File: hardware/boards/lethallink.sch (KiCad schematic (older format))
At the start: 11 parts, among them J1 PCIe-x4

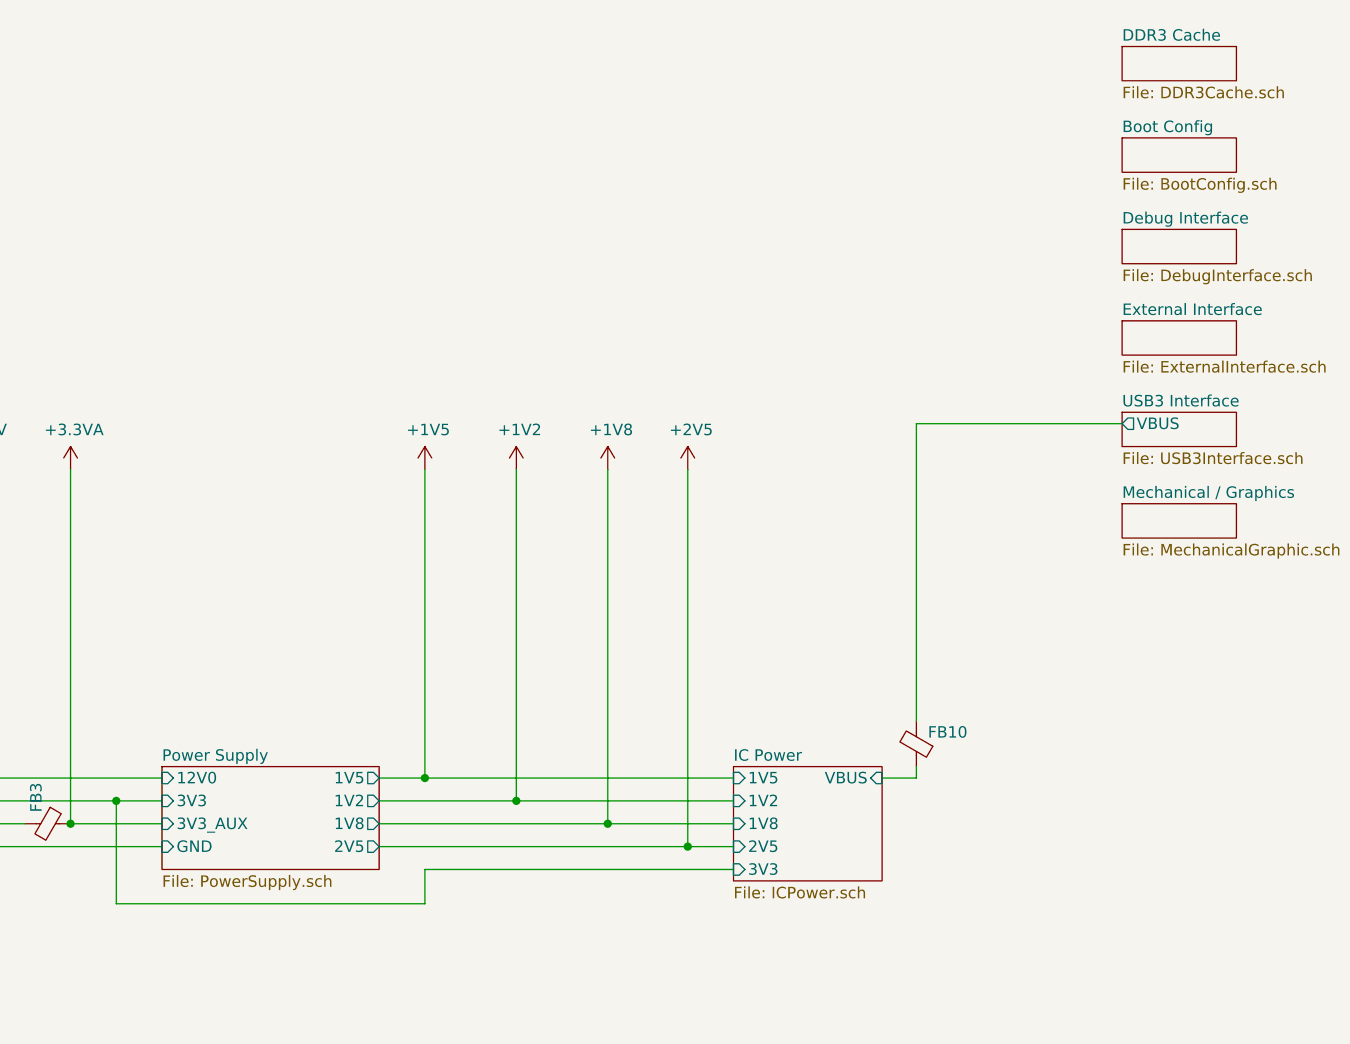
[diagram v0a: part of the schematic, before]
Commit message: Added the JTAG header and some misc cleanup
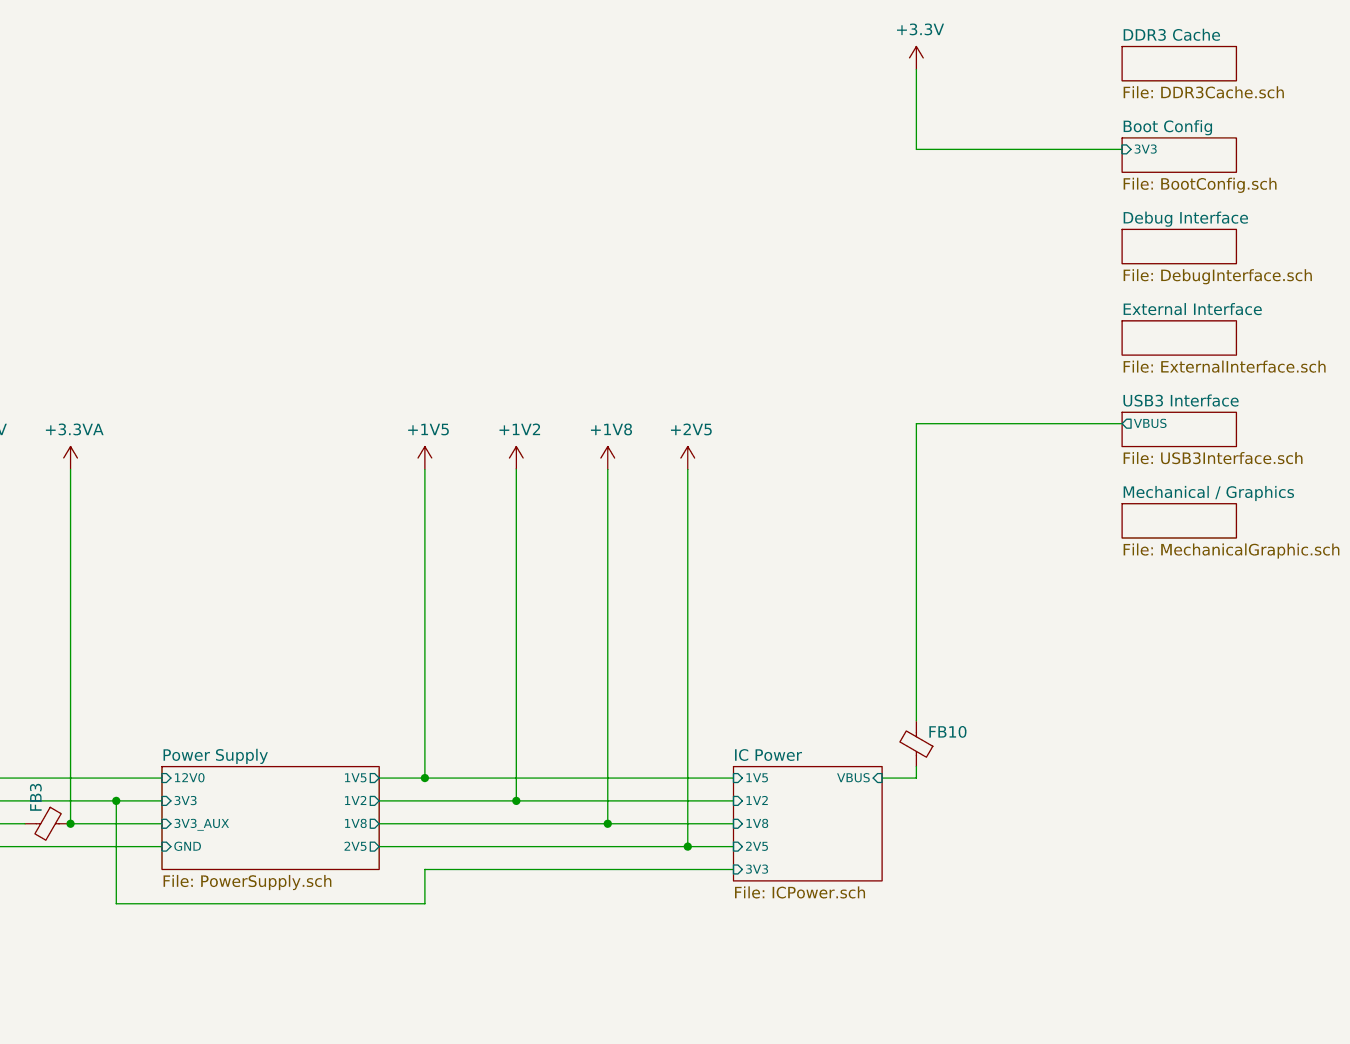
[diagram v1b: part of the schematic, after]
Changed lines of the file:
@@
 F0 "USB3 Interface" 50
 F1 "USB3Interface.sch" 50
-F2 "VBUS" O L 14700 2350 50
+F2 "VBUS" O L 14700 2350 39
 $EndSheet
 $Sheet
@@
 F0 "IC Power" 50
 F1 "ICPower.sch" 50
-F2 "3V3" I L 13000 4300 50
-F3 "1V8" I L 13000 4100 50
-F4 "2V5" I L 13000 4200 50
-F5 "1V2" I L 13000 4000 50
-F6 "1V5" I L 13000 3900 50
-F7 "VBUS" I R 13650 3900 50
+F2 "3V3" I L 13000 4300 39
+F3 "1V8" I L 13000 4100 39
+F4 "2V5" I L 13000 4200 39
+F5 "1V2" I L 13000 4000 39
+F6 "1V5" I L 13000 3900 39
+F7 "VBUS" I R 13650 3900 39
 $EndSheet
 $Comp
@@
 F0 "Power Supply" 50
 F1 "PowerSupply.sch" 50
-F2 "12V0" I L 10500 3900 50
-F3 "3V3" I L 10500 4000 50
-F4 "3V3_AUX" I L 10500 4100 50
-F5 "GND" I L 10500 4200 50
-F6 "1V2" O R 11450 4000 50
-F7 "2V5" O R 11450 4200 50
-F8 "1V8" O R 11450 4100 50
-F9 "1V5" O R 11450 3900 50
+F2 "12V0" I L 10500 3900 39
+F3 "3V3" I L 10500 4000 39
+F4 "3V3_AUX" I L 10500 4100 39
+F5 "GND" I L 10500 4200 39
+F6 "1V2" O R 11450 4000 39
+F7 "2V5" O R 11450 4200 39
+F8 "1V8" O R 11450 4100 39
+F9 "1V5" O R 11450 3900 39
 $EndSheet
 Wire Wire Line
@@
 	1    0    0    -1
 $EndComp
-$Sheet
-S 14700 1100 500  150
-U 5EF66251
-F0 "Boot Config" 50
-F1 "BootConfig.sch" 50
-$EndSheet
 Connection ~ 8950 4200
 $Comp
@@
 F1 "DDR3Cache.sch" 50
 $EndSheet
+$Sheet
+S 14700 1100 500  150
+U 5EF66251
+F0 "Boot Config" 50
+F1 "BootConfig.sch" 50
+F2 "3V3" I L 14700 1150 39
+$EndSheet
+Wire Wire Line
+	13800 800  13800 1150
+$Comp
+L power:+3.3V #PWR0126
+U 1 1 5FDBB3B1
+P 13800 800
+F 0 "#PWR0126" H 13800 650 50  0001 C CNN
+F 1 "+3.3V" H 13815 973 50  0000 C CNN
+F 2 "" H 13800 800 50  0001 C CNN
+F 3 "" H 13800 800 50  0001 C CNN
+	1    13800 800
+	1    0    0    -1
+$EndComp
+Wire Wire Line
+	13800 1150 14700 1150
 $EndSCHEMATC

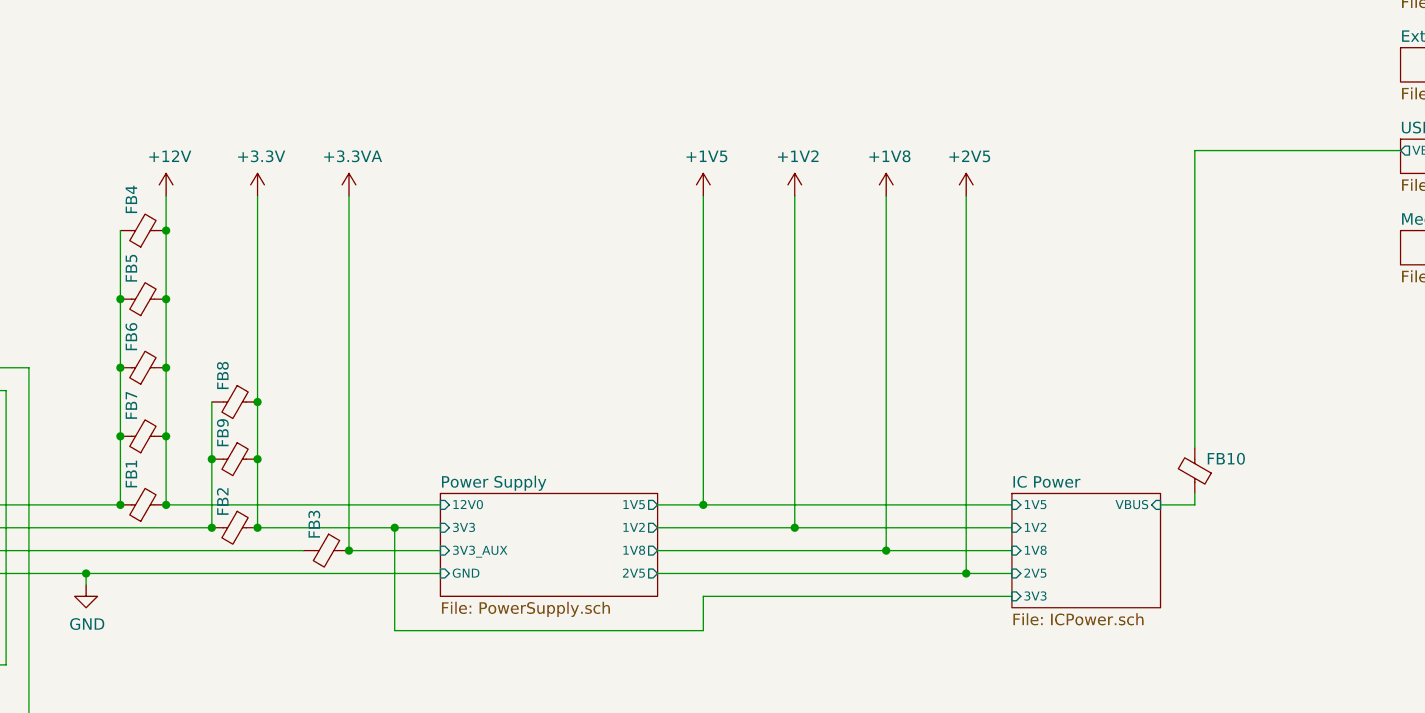
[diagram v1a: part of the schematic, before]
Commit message: Some ERC cleanup
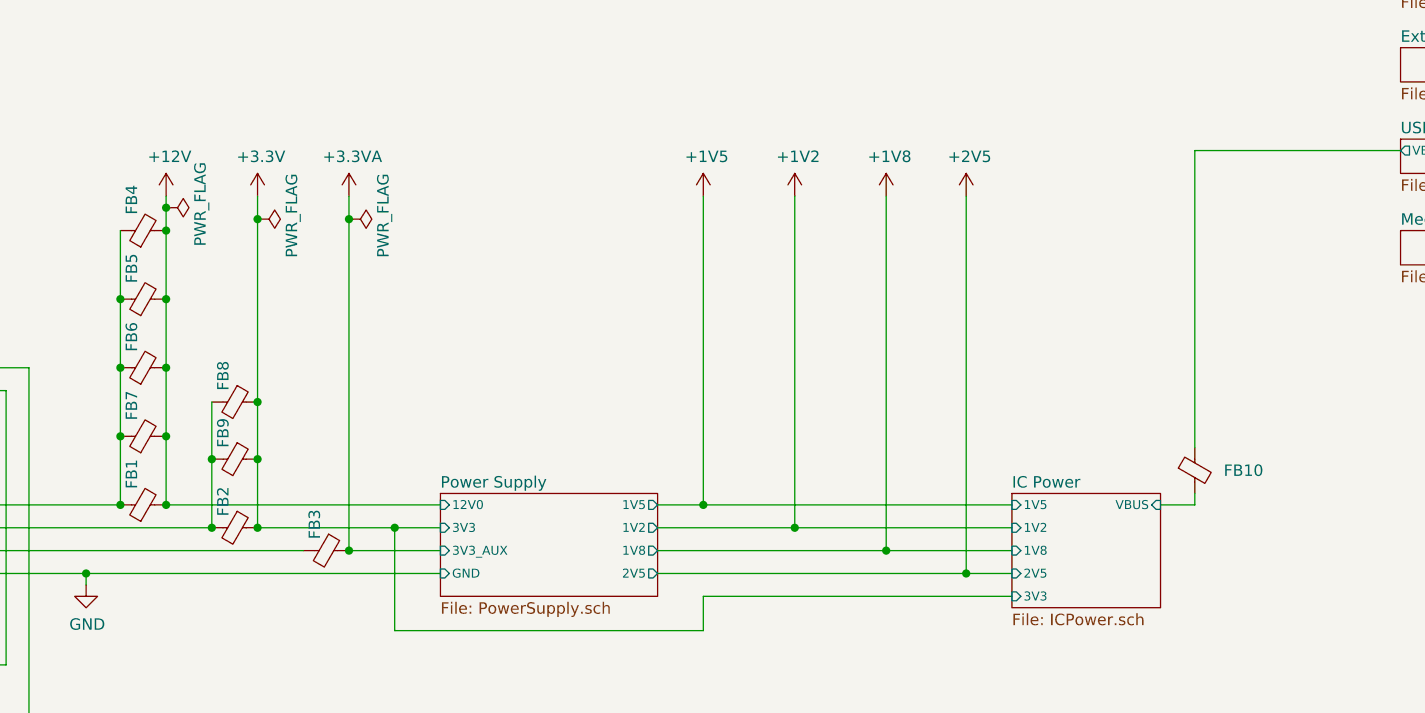
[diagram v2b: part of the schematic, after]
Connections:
- net IC Power/VBUS: now also FB10.2; no longer FB10.1
- net USB3 Interface/VBUS: now also FB10.1; no longer FB10.2
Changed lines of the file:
@@
 $EndComp
 Wire Wire Line
-	9700 2550 9700 3450
-Wire Wire Line
-	9300 2550 9300 2700
+	9700 2550 9700 2650
+Wire Wire Line
+	9300 2550 9300 2600
 $Comp
 L power:+1V5 #PWR0105
@@
 	9700 3450 9700 3700
 Wire Wire Line
-	10100 2550 10100 4100
+	10100 2550 10100 2650
 Connection ~ 9300 3900
 $Comp
@@
 U 1 1 5F74D6CA
 P 13800 3750
-F 0 "FB10" H 13750 3700 50  0000 R CNN
+F 0 "FB10" H 14100 3750 50  0000 R CNN
 F 1 "220 @ 100Mhz" H 13950 3950 50  0001 R CNN
 F 2 "Resistor_SMD:R_0603_1608Metric" V 13730 3750 50  0001 C CNN
@@
 F 5 "BLM18AG221SN1D" H 13800 3750 50  0001 C CNN "MPN"
 	1    13800 3750
-	-1   0    0    1
+	1    0    0    -1
 $EndComp
 Wire Wire Line
@@
 Wire Wire Line
 	13800 1150 14700 1150
+$Comp
+L power:PWR_FLAG #FLG0101
+U 1 1 60506733
+P 9300 2600
+F 0 "#FLG0101" H 9300 2675 50  0001 C CNN
+F 1 "PWR_FLAG" H 9100 2750 50  0000 L CNN
+F 2 "" H 9300 2600 50  0001 C CNN
+F 3 "~" H 9300 2600 50  0001 C CNN
+	1    9300 2600
+	0    1    1    0
+$EndComp
+Connection ~ 9300 2600
+Wire Wire Line
+	9300 2600 9300 2700
+$Comp
+L power:PWR_FLAG #FLG0102
+U 1 1 6050B2D3
+P 9700 2650
+F 0 "#FLG0102" H 9700 2725 50  0001 C CNN
+F 1 "PWR_FLAG" H 9500 2800 50  0000 L CNN
+F 2 "" H 9700 2650 50  0001 C CNN
+F 3 "~" H 9700 2650 50  0001 C CNN
+	1    9700 2650
+	0    1    1    0
+$EndComp
+Connection ~ 9700 2650
+Wire Wire Line
+	9700 2650 9700 3450
+$Comp
+L power:PWR_FLAG #FLG0103
+U 1 1 6050B60E
+P 10100 2650
+F 0 "#FLG0103" H 10100 2725 50  0001 C CNN
+F 1 "PWR_FLAG" H 9900 2800 50  0000 L CNN
+F 2 "" H 10100 2650 50  0001 C CNN
+F 3 "~" H 10100 2650 50  0001 C CNN
+	1    10100 2650
+	0    1    1    0
+$EndComp
+Connection ~ 10100 2650
+Wire Wire Line
+	10100 2650 10100 4100
 $EndSCHEMATC

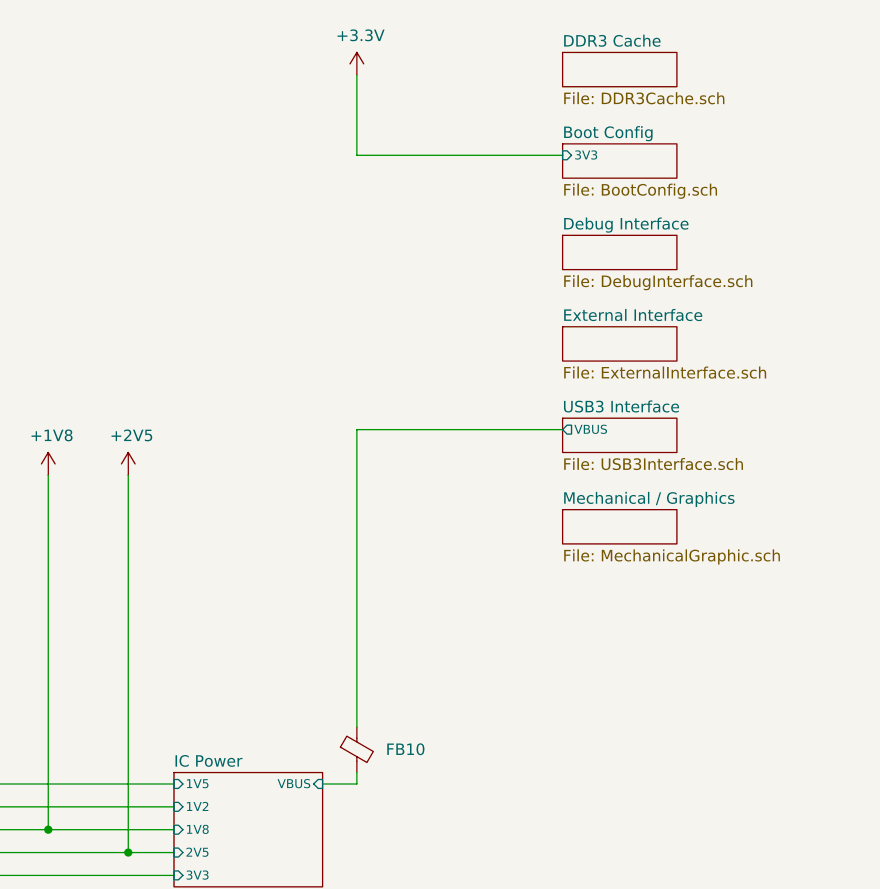
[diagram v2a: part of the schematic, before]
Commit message: Resized some nested schematics and pulled the GPIF II interrupt line out from the boot config block into the USB 3 interface
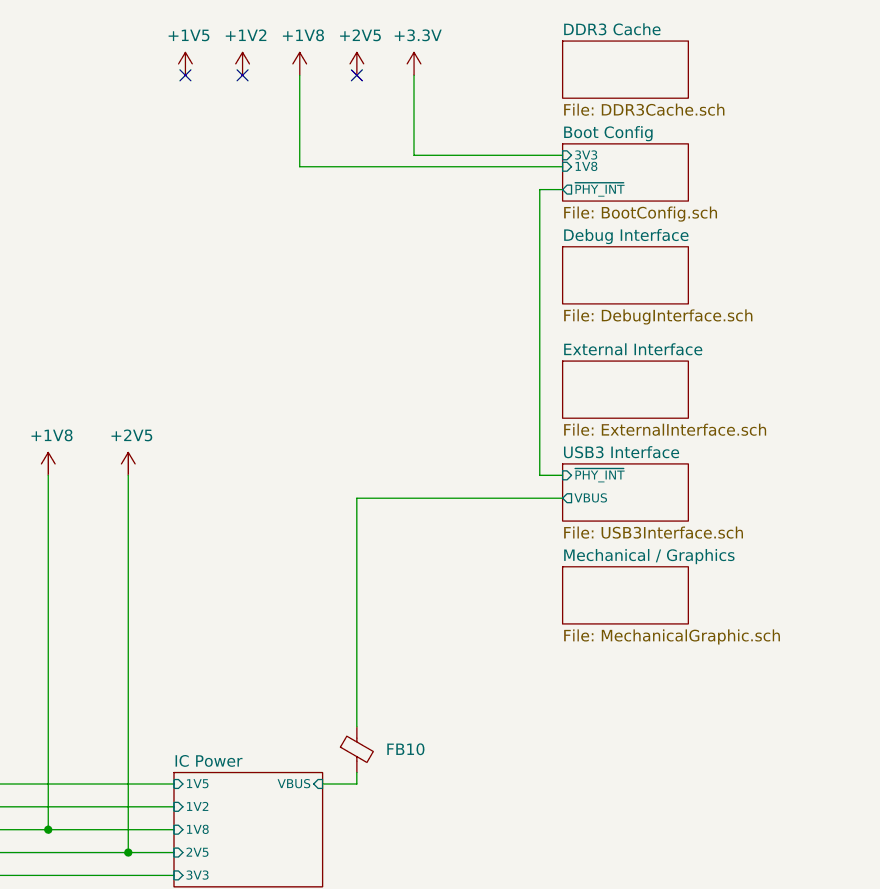
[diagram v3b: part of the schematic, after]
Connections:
- no-connect marks 2 -> 5
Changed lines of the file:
@@
 $EndDescr
 $Sheet
-S 14700 2300 500  150
-U 5F2CAFD2
-F0 "USB3 Interface" 50
-F1 "USB3Interface.sch" 50
-F2 "VBUS" O L 14700 2350 39
-$EndSheet
-$Sheet
-S 14700 1900 500  150
+S 14700 2050 550  250
 U 5EF6A128
 F0 "External Interface" 50
@@
 $EndSheet
 $Sheet
-S 14700 1500 500  150
+S 14700 1550 550  250
 U 5EF67D90
 F0 "Debug Interface" 50
@@
 $EndSheet
 $Sheet
-S 14700 2700 500  150
+S 14700 2950 550  250
 U 5F55EF4C
 F0 "Mechanical / Graphics" 50
@@
 	13650 3900 13800 3900
 Wire Wire Line
-	13800 3650 13800 2350
-Wire Wire Line
-	13800 2350 14700 2350
-Wire Wire Line
 	12450 2550 12450 4100
 Wire Wire Line
@@
 	8350 3900 9100 3900
 $Sheet
-S 14700 700  500  150
+S 14700 650  550  250
 U 5EDF3898
 F0 "DDR3 Cache" 50
@@
 $EndSheet
 $Sheet
-S 14700 1100 500  150
+S 14700 1100 550  250
 U 5EF66251
 F0 "Boot Config" 50
 F1 "BootConfig.sch" 50
 F2 "3V3" I L 14700 1150 39
-$EndSheet
-Wire Wire Line
-	13800 800  13800 1150
+F3 "1V8" I L 14700 1200 39
+F4 "~PHY_INT" O L 14700 1300 39
+$EndSheet
+Wire Wire Line
+	14050 800  14050 1150
 $Comp
 L power:+3.3V #PWR0126
 U 1 1 5FDBB3B1
-P 13800 800
-F 0 "#PWR0126" H 13800 650 50  0001 C CNN
-F 1 "+3.3V" H 13815 973 50  0000 C CNN
-F 2 "" H 13800 800 50  0001 C CNN
-F 3 "" H 13800 800 50  0001 C CNN
-	1    13800 800
-	1    0    0    -1
-$EndComp
-Wire Wire Line
-	13800 1150 14700 1150
+P 14050 800
+F 0 "#PWR0126" H 14050 650 50  0001 C CNN
+F 1 "+3.3V" H 14065 973 50  0000 C CNN
+F 2 "" H 14050 800 50  0001 C CNN
+F 3 "" H 14050 800 50  0001 C CNN
+	1    14050 800
+	1    0    0    -1
+$EndComp
+Wire Wire Line
+	14050 1150 14700 1150
 $Comp
 L power:PWR_FLAG #FLG0101
@@
 Wire Wire Line
 	10100 2650 10100 4100
+$Comp
+L power:+1V8 #PWR?
+U 1 1 60A4DFF4
+P 13550 800
+AR Path="/5EDF9F51/60A4DFF4" Ref="#PWR?"  Part="1"
+AR Path="/60A4DFF4" Ref="#PWR0132"  Part="1"
+F 0 "#PWR0132" H 13550 650 50  0001 C CNN
+F 1 "+1V8" H 13565 973 50  0000 C CNN
+F 2 "" H 13550 800 50  0001 C CNN
+F 3 "" H 13550 800 50  0001 C CNN
+	1    13550 800
+	1    0    0    -1
+$EndComp
+$Comp
+L power:+2V5 #PWR?
+U 1 1 60A551C4
+P 13800 800
+AR Path="/5EDF9F51/60A551C4" Ref="#PWR?"  Part="1"
+AR Path="/60A551C4" Ref="#PWR0133"  Part="1"
+F 0 "#PWR0133" H 13800 650 50  0001 C CNN
+F 1 "+2V5" H 13815 973 50  0000 C CNN
+F 2 "" H 13800 800 50  0001 C CNN
+F 3 "" H 13800 800 50  0001 C CNN
+	1    13800 800
+	1    0    0    -1
+$EndComp
+$Comp
+L power:+1V5 #PWR0134
+U 1 1 60A665A9
+P 13050 800
+F 0 "#PWR0134" H 13050 650 50  0001 C CNN
+F 1 "+1V5" H 13065 973 50  0000 C CNN
+F 2 "" H 13050 800 50  0001 C CNN
+F 3 "" H 13050 800 50  0001 C CNN
+	1    13050 800
+	1    0    0    -1
+$EndComp
+$Comp
+L power:+1V2 #PWR?
+U 1 1 60A665AF
+P 13300 800
+AR Path="/5EDF9F51/60A665AF" Ref="#PWR?"  Part="1"
+AR Path="/60A665AF" Ref="#PWR0135"  Part="1"
+F 0 "#PWR0135" H 13300 650 50  0001 C CNN
+F 1 "+1V2" H 13315 973 50  0000 C CNN
+F 2 "" H 13300 800 50  0001 C CNN
+F 3 "" H 13300 800 50  0001 C CNN
+	1    13300 800
+	1    0    0    -1
+$EndComp
+Wire Wire Line
+	13550 1200 13550 800
+Wire Wire Line
+	13550 1200 14700 1200
+NoConn ~ 13800 800
+NoConn ~ 13300 800
+NoConn ~ 13050 800
+Wire Wire Line
+	13800 3650 13800 2650
+Wire Wire Line
+	13800 2650 14700 2650
+$Sheet
+S 14700 2500 550  250
+U 5F2CAFD2
+F0 "USB3 Interface" 50
+F1 "USB3Interface.sch" 50
+F2 "VBUS" O L 14700 2650 39
+F3 "~PHY_INT" I L 14700 2550 39
+$EndSheet
+Wire Wire Line
+	14700 1300 14600 1300
+Wire Wire Line
+	14600 1300 14600 2550
+Wire Wire Line
+	14600 2550 14700 2550
 $EndSCHEMATC
